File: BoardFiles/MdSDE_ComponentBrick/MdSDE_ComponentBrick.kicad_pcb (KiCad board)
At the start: 2 copper layers, 50 parts, among them P101 CONN_01X10, P102 CONN_01X10, SW201 Coded_Switch, SW202 SPST_x3, SW301 Coded_Switch, SW302 SPST_x3, SW401 Coded_Switch, SW402 SPST_x3, SW501 Coded_Switch, SW502 SPST_x3, SW601 Coded_Switch, SW602 SPST_x3, SW701 Coded_Switch, SW702 SPST_x3, SW801 Coded_Switch, SW802 SPST_x3, SW901 Coded_Switch, SW902 SPST_x3

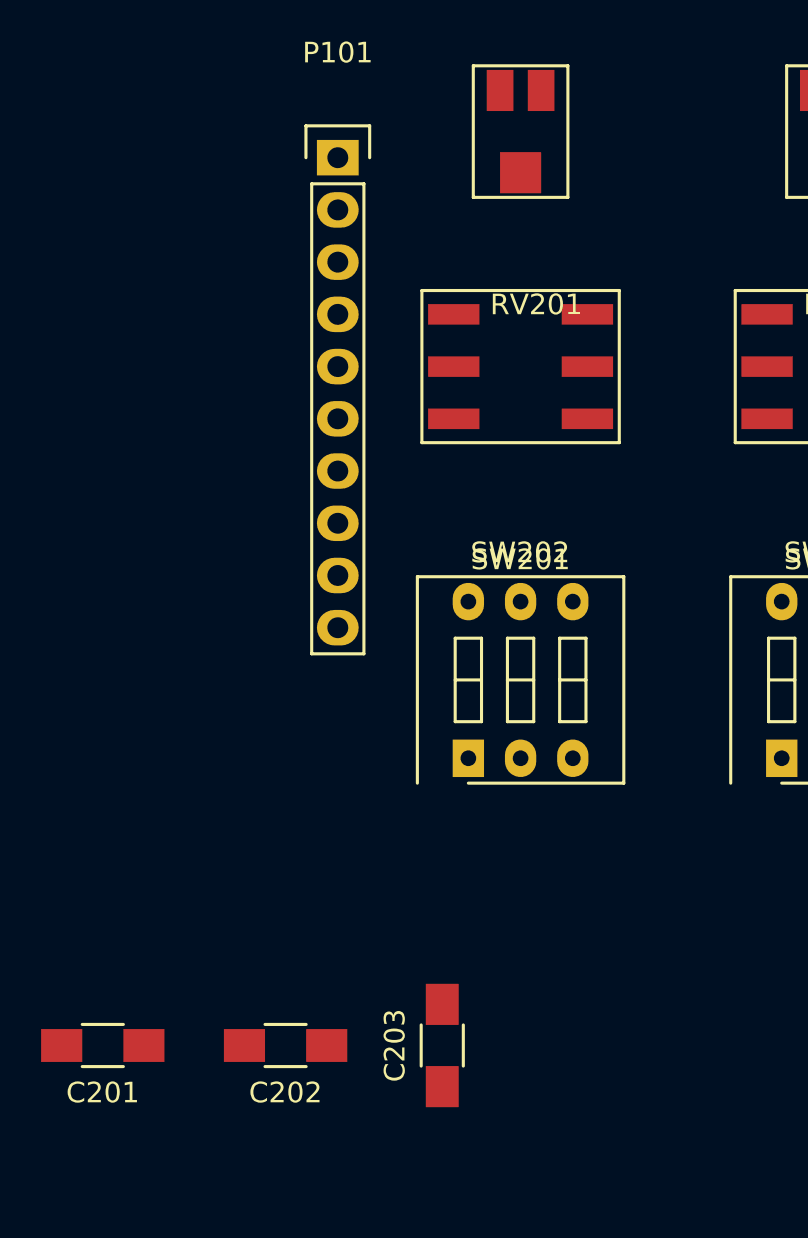
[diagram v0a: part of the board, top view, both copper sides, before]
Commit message: Checked layout, placed three caps
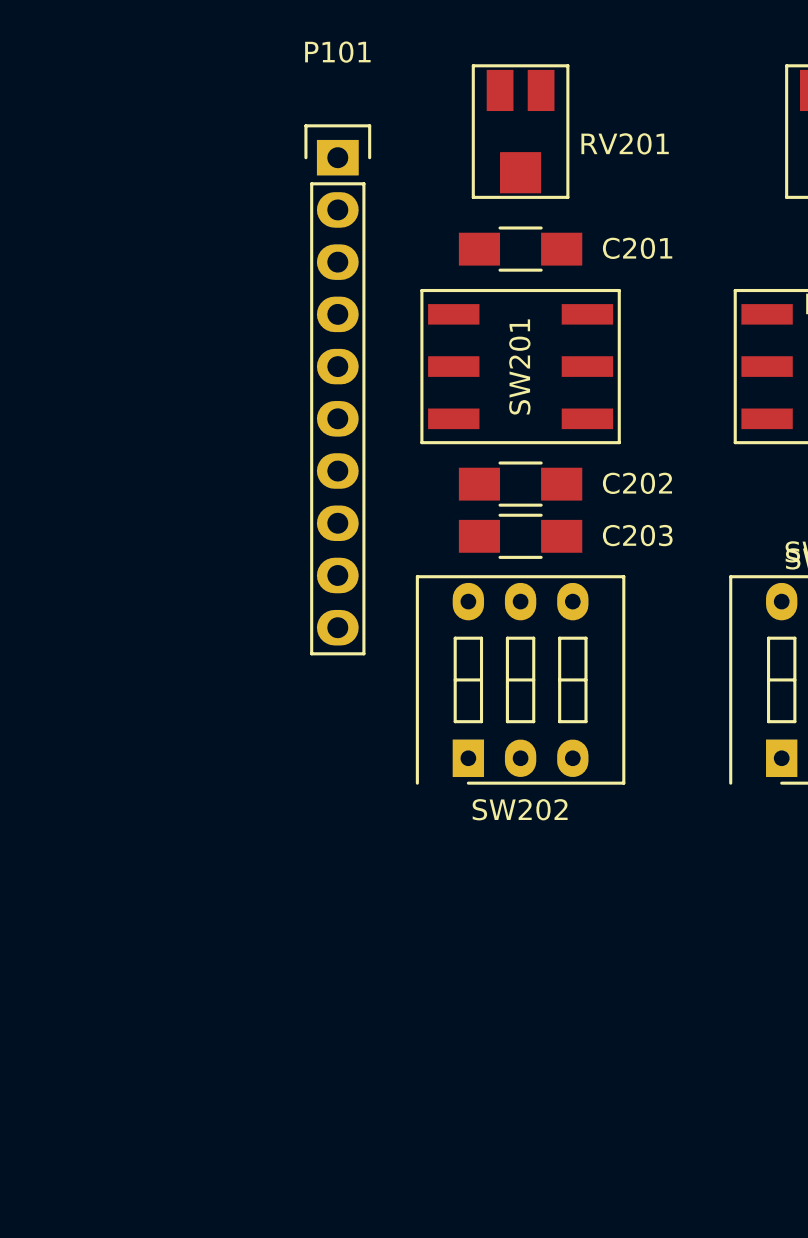
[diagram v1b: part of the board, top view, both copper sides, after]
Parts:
- moved C201 43.7 mm to (86.4, 74.3), turned to 0 degrees
- moved C202 29.6 mm to (86.4, 85.7)
- moved C203 25.1 mm to (86.4, 88.3), turned to 180 degrees
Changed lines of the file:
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@@
-(kicad_pcb (version 4) (host pcbnew 4.0.1-stable)
+(kicad_pcb (version 4) (host pcbnew 4.0.0-stable)
   (general
     (links 115)
     (no_connects 115)
-    (area 85.823667 71.679 223.489001 191.467)
+    (area 62.514999 54.3 223.489001 167.867)
     (thickness 1.6)
     (drawings 2)
@@
     (pad_to_mask_clearance 0.2)
     (aux_axis_origin 0 0)
-    (visible_elements FFFFF77F)
+    (visible_elements 7FFEF7FF)
     (pcbplotparams
       (layerselection 0x00030_80000001)
@@
   )
   (module Capacitors_SMD:C_1206_HandSoldering (layer F.Cu)
-    (at 66.04 113.03 180)
-    (descr "Capacitor SMD 1206, hand soldering")
-    (tags "capacitor 1206")
-    (attr smd)
-    (fp_text reference C201 (at 0 -2.3 180) (layer F.SilkS)
-      (effects (font (size 1 1) (thickness 0.15)))
-    )
-    (fp_text value C_Small (at 0 2.3 180) (layer F.Fab)
-      (effects (font (size 1 1) (thickness 0.15)))
-    )
-    (fp_line (start -3.3 -1.15) (end 3.3 -1.15) (layer F.CrtYd) (width 0.05))
-    (fp_line (start -3.3 1.15) (end 3.3 1.15) (layer F.CrtYd) (width 0.05))
-    (fp_line (start -3.3 -1.15) (end -3.3 1.15) (layer F.CrtYd) (width 0.05))
-    (fp_line (start 3.3 -1.15) (end 3.3 1.15) (layer F.CrtYd) (width 0.05))
-    (fp_line (start 1 -1.025) (end -1 -1.025) (layer F.SilkS) (width 0.15))
-    (fp_line (start -1 1.025) (end 1 1.025) (layer F.SilkS) (width 0.15))
-    (pad 1 smd rect (at -2 0 180) (size 2 1.6) (layers F.Cu F.Paste F.Mask)
+    (at 86.36 74.295)
+    (descr "Capacitor SMD 1206, hand soldering")
+    (tags "capacitor 1206")
+    (attr smd)
+    (fp_text reference C201 (at 5.715 0) (layer F.SilkS)
+      (effects (font (size 1 1) (thickness 0.15)))
+    )
+    (fp_text value C_Small (at 0 -1.905) (layer F.Fab)
+      (effects (font (size 1 1) (thickness 0.15)))
+    )
+    (fp_line (start -3.3 -1.15) (end 3.3 -1.15) (layer F.CrtYd) (width 0.05))
+    (fp_line (start -3.3 1.15) (end 3.3 1.15) (layer F.CrtYd) (width 0.05))
+    (fp_line (start -3.3 -1.15) (end -3.3 1.15) (layer F.CrtYd) (width 0.05))
+    (fp_line (start 3.3 -1.15) (end 3.3 1.15) (layer F.CrtYd) (width 0.05))
+    (fp_line (start 1 -1.025) (end -1 -1.025) (layer F.SilkS) (width 0.15))
+    (fp_line (start -1 1.025) (end 1 1.025) (layer F.SilkS) (width 0.15))
+    (pad 1 smd rect (at -2 0) (size 2 1.6) (layers F.Cu F.Paste F.Mask)
       (net 1 "Net-(C201-Pad1)"))
-    (pad 2 smd rect (at 2 0 180) (size 2 1.6) (layers F.Cu F.Paste F.Mask)
-      (net 2 GND))
-    (model Capacitors_SMD.3dshapes/C_1206_HandSoldering.wrl
-      (at (xyz 0 0 0))
-      (scale (xyz 1 1 1))
-      (rotate (xyz 0 0 0))
-    )
-  )
-  (module Capacitors_SMD:C_1206_HandSoldering (layer F.Cu)
-    (at 74.93 113.03 180)
-    (descr "Capacitor SMD 1206, hand soldering")
-    (tags "capacitor 1206")
-    (attr smd)
-    (fp_text reference C202 (at 0 -2.3 180) (layer F.SilkS)
-      (effects (font (size 1 1) (thickness 0.15)))
-    )
-    (fp_text value C_Small (at 0 2.3 180) (layer F.Fab)
+    (pad 2 smd rect (at 2 0) (size 2 1.6) (layers F.Cu F.Paste F.Mask)
+      (net 2 GND))
+    (model Capacitors_SMD.3dshapes/C_1206_HandSoldering.wrl
+      (at (xyz 0 0 0))
+      (scale (xyz 1 1 1))
+      (rotate (xyz 0 0 0))
+    )
+  )
+  (module Capacitors_SMD:C_1206_HandSoldering (layer F.Cu)
+    (at 86.36 85.725 180)
+    (descr "Capacitor SMD 1206, hand soldering")
+    (tags "capacitor 1206")
+    (attr smd)
+    (fp_text reference C202 (at -5.715 0 180) (layer F.SilkS)
+      (effects (font (size 1 1) (thickness 0.15)))
+    )
+    (fp_text value C_Small (at 0 1.905 180) (layer F.Fab)
       (effects (font (size 1 1) (thickness 0.15)))
     )
@@
   )
   (module Capacitors_SMD:C_1206_HandSoldering (layer F.Cu)
-    (at 82.55 113.03 90)
-    (descr "Capacitor SMD 1206, hand soldering")
-    (tags "capacitor 1206")
-    (attr smd)
-    (fp_text reference C203 (at 0 -2.3 90) (layer F.SilkS)
-      (effects (font (size 1 1) (thickness 0.15)))
-    )
-    (fp_text value C_Small (at 0 2.3 90) (layer F.Fab)
-      (effects (font (size 1 1) (thickness 0.15)))
-    )
-    (fp_line (start -3.3 -1.15) (end 3.3 -1.15) (layer F.CrtYd) (width 0.05))
-    (fp_line (start -3.3 1.15) (end 3.3 1.15) (layer F.CrtYd) (width 0.05))
-    (fp_line (start -3.3 -1.15) (end -3.3 1.15) (layer F.CrtYd) (width 0.05))
-    (fp_line (start 3.3 -1.15) (end 3.3 1.15) (layer F.CrtYd) (width 0.05))
-    (fp_line (start 1 -1.025) (end -1 -1.025) (layer F.SilkS) (width 0.15))
-    (fp_line (start -1 1.025) (end 1 1.025) (layer F.SilkS) (width 0.15))
-    (pad 1 smd rect (at -2 0 90) (size 2 1.6) (layers F.Cu F.Paste F.Mask)
+    (at 86.36 88.265 180)
+    (descr "Capacitor SMD 1206, hand soldering")
+    (tags "capacitor 1206")
+    (attr smd)
+    (fp_text reference C203 (at -5.715 0 180) (layer F.SilkS)
+      (effects (font (size 1 1) (thickness 0.15)))
+    )
+    (fp_text value C_Small (at 0 1.27 180) (layer F.Fab)
+      (effects (font (size 1 1) (thickness 0.15)))
+    )
+    (fp_line (start -3.3 -1.15) (end 3.3 -1.15) (layer F.CrtYd) (width 0.05))
+    (fp_line (start -3.3 1.15) (end 3.3 1.15) (layer F.CrtYd) (width 0.05))
+    (fp_line (start -3.3 -1.15) (end -3.3 1.15) (layer F.CrtYd) (width 0.05))
+    (fp_line (start 3.3 -1.15) (end 3.3 1.15) (layer F.CrtYd) (width 0.05))
+    (fp_line (start 1 -1.025) (end -1 -1.025) (layer F.SilkS) (width 0.15))
+    (fp_line (start -1 1.025) (end 1 1.025) (layer F.SilkS) (width 0.15))
+    (pad 1 smd rect (at -2 0 180) (size 2 1.6) (layers F.Cu F.Paste F.Mask)
       (net 4 "Net-(C203-Pad1)"))
-    (pad 2 smd rect (at 2 0 90) (size 2 1.6) (layers F.Cu F.Paste F.Mask)
+    (pad 2 smd rect (at 2 0 180) (size 2 1.6) (layers F.Cu F.Paste F.Mask)
       (net 2 GND))
     (model Capacitors_SMD.3dshapes/C_1206_HandSoldering.wrl
@@
   (module Footprints:SH-7000RotarySwitch (layer F.Cu)
     (at 86.36 80.01)
-    (fp_text reference SW201 (at 0 9.39) (layer F.SilkS)
-      (effects (font (size 1 1) (thickness 0.15)))
-    )
-    (fp_text value Coded_Switch (at 0 8.39) (layer F.Fab)
+    (fp_text reference SW201 (at 0 0 90) (layer F.SilkS)
+      (effects (font (size 1 1) (thickness 0.15)))
+    )
+    (fp_text value Coded_Switch (at 0 22.86) (layer F.Fab)
       (effects (font (size 1 1) (thickness 0.15)))
     )
@@
     (at 83.82 99.06)
     (descr "CTS Electrocomponents, Series 206/208")
-    (fp_text reference SW202 (at 2.52 -10) (layer F.SilkS)
+    (fp_text reference SW202 (at 2.54 2.54) (layer F.SilkS)
       (effects (font (size 1 1) (thickness 0.15)))
     )
@@
   (module Footprints:3314_Potentiometer (layer F.Cu)
     (at 86.36 68.58)
-    (fp_text reference RV201 (at 0.77 8.42) (layer F.SilkS)
-      (effects (font (size 1 1) (thickness 0.15)))
-    )
+    (fp_text reference RV201 (at 5.08 0.635) (layer F.SilkS)
+      (effects (font (size 1 1) (thickness 0.15)))
+    )

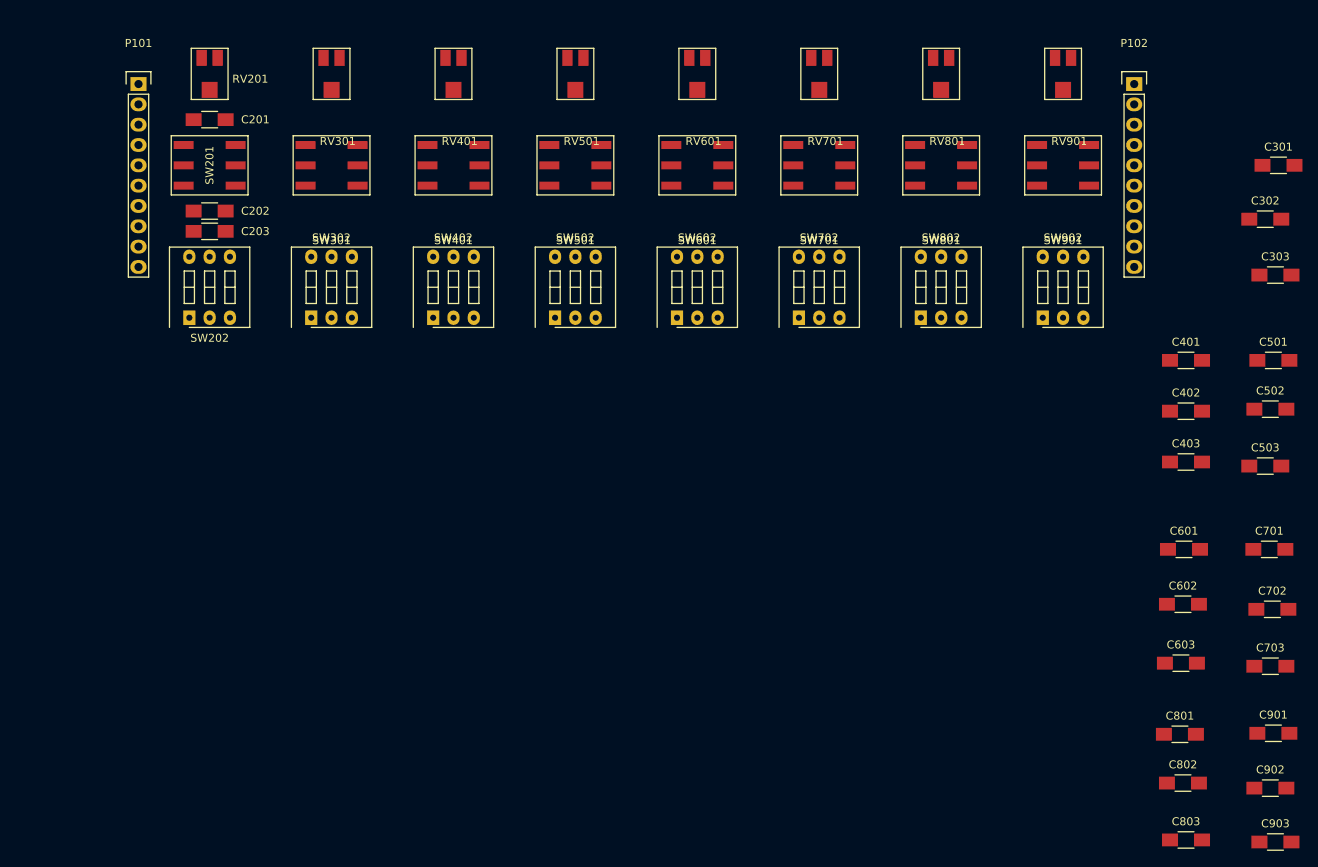
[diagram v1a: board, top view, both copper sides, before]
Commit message: updated layout
updated layout without traces
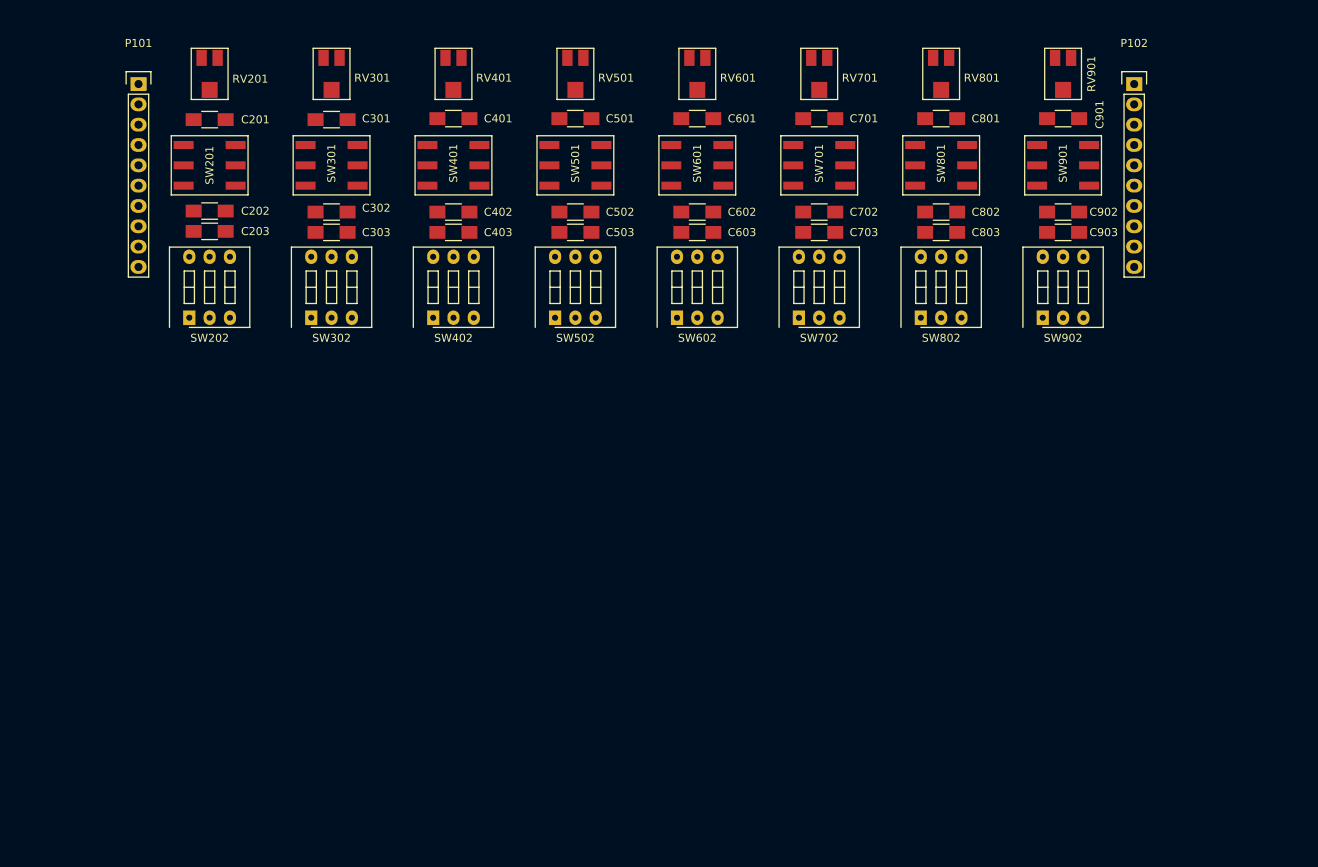
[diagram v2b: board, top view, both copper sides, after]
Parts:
- moved C301 118.5 mm to (101.6, 74.3)
- moved C303 118.1 mm to (101.6, 88.4)
- moved C302 116.7 mm to (101.6, 85.9)
- moved C401 96.4 mm to (116.8, 74.2)
- moved C403 96.0 mm to (116.8, 88.4)
- moved C402 94.9 mm to (116.8, 85.9)
- moved C501 92.3 mm to (132.1, 74.2)
- moved C503 91.0 mm to (132.1, 88.4)
- moved C502 90.3 mm to (132.1, 85.9)
- moved C801 82.5 mm to (177.8, 74.2)
- moved C803 81.9 mm to (177.8, 88.4)
- moved C601 81.2 mm to (147.3, 74.2)
- moved C901 81.2 mm to (193.0, 74.2)
- moved C603 81.0 mm to (147.3, 88.4)
- moved C903 80.7 mm to (193.0, 88.4)
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
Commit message: updated pcb routing traces
began the process of routing traces
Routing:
- net GND: track 0.00 -> 297.9 mm, vias 0 -> 15
- net Net-(RV201-Pad1): track 0.00 -> 46.2 mm, vias 0 -> 1
- net Net-(RV201-Pad2): track 0.00 -> 33.9 mm, vias 0 -> 1
- net Net-(C201-Pad1): track 0.00 -> 6.07 mm

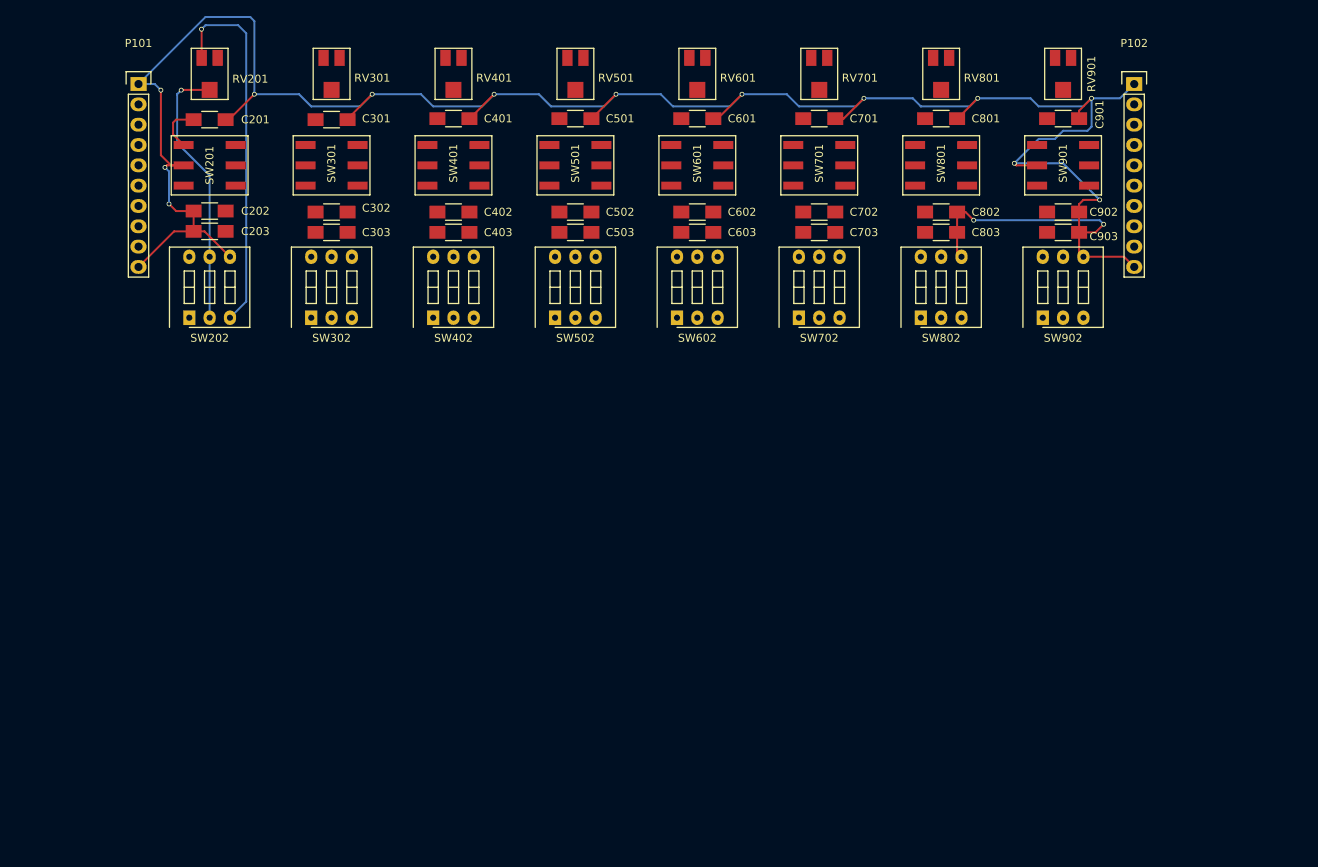
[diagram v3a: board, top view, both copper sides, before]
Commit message: updated traces
more work on the tracks
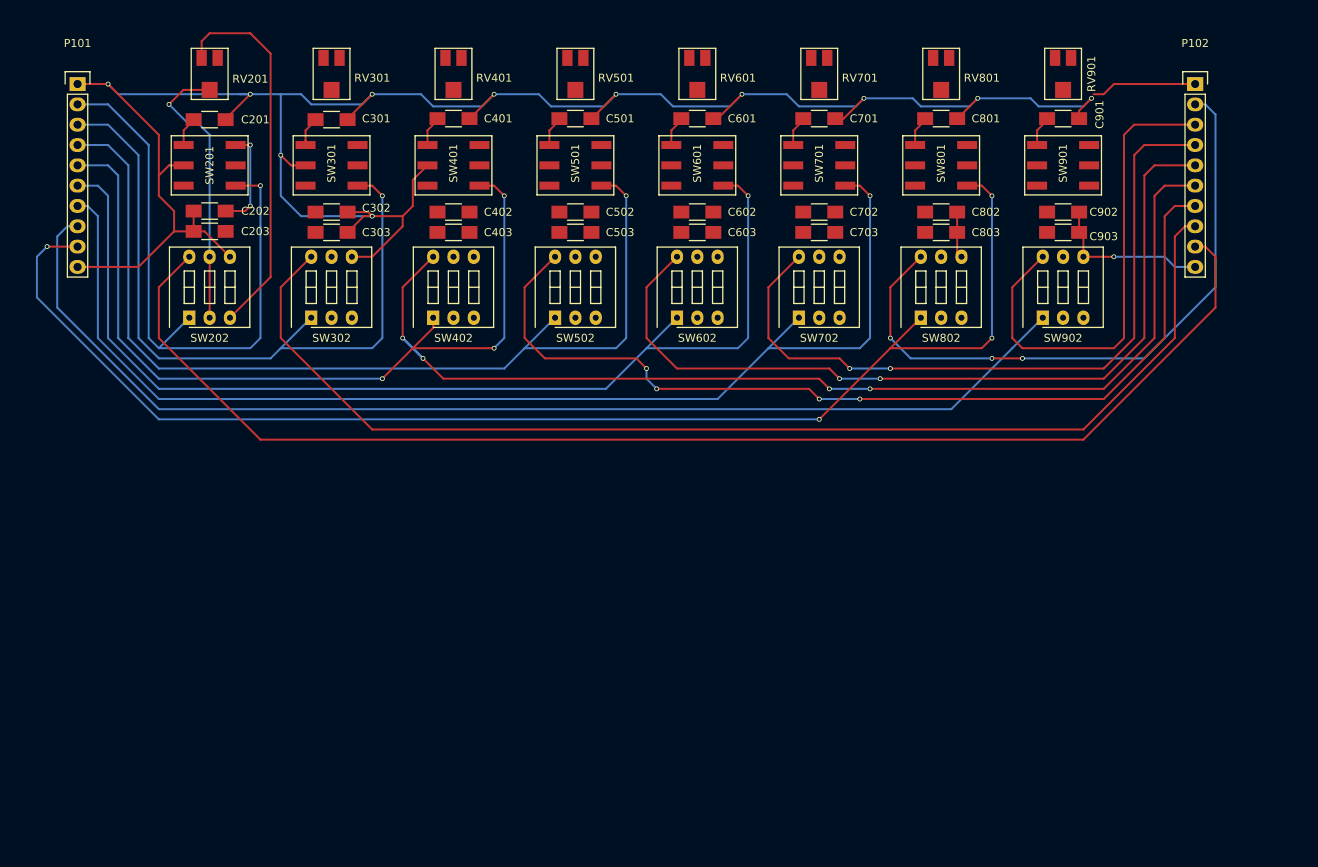
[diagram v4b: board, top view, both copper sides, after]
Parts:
- moved P101 7.62 mm to (69.8, 69.8)
- moved P102 7.62 mm to (209.6, 69.8)
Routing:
- net Pin8: track 0.00 -> 167.4 mm, vias 0 -> 4
- net Src1: track 0.00 -> 165.3 mm
- net Src2: track 0.00 -> 148.7 mm
- net Pin6: track 0.00 -> 147.9 mm, vias 0 -> 1
- net Pin7: track 0.00 -> 145.1 mm
- net Src4: track 0.00 -> 138.0 mm, vias 0 -> 4
- net Pin5: track 0.00 -> 134.2 mm, vias 0 -> 1
- net Pin3: track 0.00 -> 121.2 mm, vias 0 -> 1
- net Src3: track 0.00 -> 118.4 mm, vias 0 -> 4
- net Src5: track 0.00 -> 105.4 mm, vias 0 -> 2
- net Pin4: track 0.00 -> 104.7 mm, vias 0 -> 3
- net Src6: track 0.00 -> 91.6 mm, vias 0 -> 2
- net Pin2: track 0.00 -> 91.4 mm, vias 0 -> 1
- net Src8: track 0.00 -> 81.8 mm, vias 0 -> 3
- net Pin1: track 0.00 -> 77.7 mm, vias 0 -> 1
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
